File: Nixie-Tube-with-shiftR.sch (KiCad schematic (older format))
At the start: 6 parts

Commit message: finalize schematic, added so16 footprint
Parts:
- removed Q?: 2N2219, TO_SOT_Packages_THT:TO-39-3, symbol 2N2219
- removed R?: 500, symbol R
- removed R?: R, symbol R
- removed U?: TPIC6595, symbol TPIC6595
- added D1: LED_CRGB, nixie-tube-fp:Rgb-Led, symbol LED_CRGB
- added J1: Conn_01x02_Female, Pin_Headers:Pin_Header_Angled_2x01_Pitch2.54mm, symbol Conn_01x02_Female
- added J2: Conn_01x06, Pin_Headers:Pin_Header_Angled_1x06_Pitch2.54mm, symbol Conn_01x06
- added Q1, Q10, Q2, Q3, Q4, Q5, Q6, Q7, Q8, Q9: 2N2219, TO_SOT_Packages_THT:TO-39-3, symbol 2N2219
- added Q11, Q12, Q13: Q_NMOS_DGS, symbol Q_NMOS_DGS
- added R1, R10, R2, R3, R4, R5, R6, R7, R8, R9: 25K, Resistors_SMD:R_0603, symbol R
- added R11, R12, R13: 500, Resistors_SMD:R_0603, symbol R
- added R14, R15, R16, R17, R18, R19, R20, R21, R22, R23: R, Resistors_SMD:R_0603, symbol R
- added U1, U3: 74HC595D, kilibs:SO16, symbol 74HC595D
- J3: renamed from J?; footprint (none) -> Pin_Headers:Pin_Header_Angled_1x02_Pitch2.54mm
- U2: renamed from U?; footprint (none) -> nixie-tube-fp:qs30-1
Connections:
- net labels added: +5V, Blue, Green, Red, n0, n1, n2, n3, n4, n5, n6, n7, n8, n9, s0, s1, s2, s3, s4, s5, s6, s7, s8, s9
- wire segments 8 -> 58
- no-connect marks 0 -> 7
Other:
- note added: "DS0"
- note added: "DS1"
- note added: "MR"
- note added: "OE"
- note added: "SHCP"
- note added: "STCP"

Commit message: associate all footprints, components are outside of board
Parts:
- removed J1: Conn_01x02_Female, Pin_Headers:Pin_Header_Angled_2x01_Pitch2.54mm, symbol Conn_01x02_Female
- removed J2: Conn_01x06, Pin_Headers:Pin_Header_Angled_1x06_Pitch2.54mm, symbol Conn_01x06
- removed J3: Conn_01x02_Female, Pin_Headers:Pin_Header_Angled_1x02_Pitch2.54mm, symbol Conn_01x02_Female
- removed Q1, Q10, Q2, Q3, Q4, Q5, Q6, Q7, Q8, Q9: 2N2219, TO_SOT_Packages_THT:TO-39-3, symbol 2N2219
- added C1, C2: 0.1uF, symbol C
- added D2: Dot_LED, symbol LED
- added J1: Conn_01x05_Male, Pin_Headers:Pin_Header_Angled_1x05_Pitch2.54mm, symbol Conn_01x05_Male
- added J2: Conn_01x01_Female, Socket_Strips:Socket_Strip_Angled_1x01_Pitch2.54mm, symbol Conn_01x01_Female
- added J3: Conn_01x05_Female, Socket_Strips:Socket_Strip_Angled_1x05_Pitch2.54mm, symbol Conn_01x05_Female
- added J4: Conn_01x01_Male, Pin_Headers:Pin_Header_Angled_1x01_Pitch2.54mm, symbol Conn_01x01_Male
- added Q1, Q10, Q2, Q3, Q4, Q5, Q6, Q7, Q8, Q9: MMBTA42LT1, TO_SOT_Packages_SMD:SOT-23, symbol Q_NPN_BEC
- added Q14: MMBTA42LT1, TO_SOT_Packages_SMD:SOT-23, symbol Q_NPN_BCE
- added R24, R25: R, Resistors_SMD:R_0603, symbol R
- added U4: MIC5219-3.3, TO_SOT_Packages_SMD:SOT-23-5, symbol MIC5219-3.3
- Q11, Q12, Q13: value Q_NMOS_DGS -> AO3400; footprint (none) -> TO_SOT_Packages_SMD:SOT-23
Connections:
- net labels added: +3.3V, +9V, 9V, Dot, MOSI, MOSI-OUT, PWREN, SCK
- net labels removed: +5V
- wire segments 58 -> 62
- no-connect marks 7 -> 4
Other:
- note removed: "DS0"
- note removed: "DS1"
- note removed: "MR"
- note removed: "OE"
- note removed: "SHCP"
- note removed: "STCP"
- moved on the sheet: D1, Q11, Q12, Q13, R11, R12, R13

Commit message: change ldo to 5V
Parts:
- removed U4: MIC5219-3.3, TO_SOT_Packages_SMD:SOT-23-5, symbol MIC5219-3.3
- added U?: MIC5219-5.0, TO_SOT_Packages_SMD:SOT-23-5, symbol MIC5219-5.0
- D2: symbol LED -> LED-RESCUE-Nixie-Tube-with-shiftR
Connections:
- net labels added: +5V
- wire segments 62 -> 77
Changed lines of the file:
@@
 EESchema Schematic File Version 2
+LIBS:Nixie-Tube-with-shiftR-rescue
 LIBS:power
 LIBS:device
 LIBS:switches
 LIBS:relays
-LIBS:motors
 LIBS:transistors
 LIBS:conn
@@
 s1
 Wire Wire Line
-	4050 3125 7325 3125
+	4050 3125 4800 3125
+Wire Wire Line
+	4800 3125 5650 3125
+Wire Wire Line
+	5650 3125 6500 3125
+Wire Wire Line
+	6500 3125 7325 3125
 Connection ~ 4800 3125
 Connection ~ 5650 3125
@@
 Connection ~ 5575 3775
 Wire Wire Line
-	4350 3775 6950 3775
+	4350 3775 4975 3775
+Wire Wire Line
+	4975 3775 5575 3775
+Wire Wire Line
+	5575 3775 6300 3775
+Wire Wire Line
+	6300 3775 6950 3775
 Connection ~ 4975 3775
 Connection ~ 6300 3775
@@
 	9700 5550 8575 5550
 Wire Wire Line
-	4625 1700 3950 1700
+	4625 1700 4475 1700
+Wire Wire Line
+	4475 1700 3950 1700
 $Comp
 L R R11
@@
 	2050 3850 3325 3850
 Wire Wire Line
-	3325 3950 2050 3950
+	3325 3950 2800 3950
+Wire Wire Line
+	2800 3950 2050 3950
 Wire Wire Line
 	3325 4050 2050 4050
 Wire Wire Line
-	2050 4150 3325 4150
+	2050 4150 2575 4150
+Wire Wire Line
+	2575 4150 3325 4150
 Wire Wire Line
 	4900 4275 5325 4275
@@
 MOSI-OUT
 $Comp
-L LED D2
+L LED-RESCUE-Nixie-Tube-with-shiftR D2
 U 1 1 59E02618
 P 8350 2975
@@
 	4300 5675 4300 5950
 Wire Wire Line
-	3700 5950 4600 5950
+	3700 5950 4300 5950
+Wire Wire Line
+	4300 5950 4600 5950
 Wire Wire Line
 	3700 5950 3700 5675
@@
 	5925 5650 5925 5925
 Wire Wire Line
-	5225 5925 6225 5925
+	5225 5925 5925 5925
+Wire Wire Line
+	5925 5925 6225 5925
 Wire Wire Line
 	5225 5925 5225 5625
@@
 $EndComp
 Wire Wire Line
-	2150 5250 2350 5250
+	2150 5250 2225 5250
+Wire Wire Line
+	2225 5250 2275 5250
+Wire Wire Line
+	2275 5250 2350 5250
 Wire Wire Line
 	2950 5250 3275 5250
 Wire Wire Line
 	3275 5250 3275 5200
-$Comp
-L MIC5219-3.3 U4
-U 1 1 59E0C8AF
-P 2650 5350
-F 0 "U4" H 2500 5575 50  0000 C CNN
-F 1 "MIC5219-3.3" H 2650 5575 50  0000 L CNN
-F 2 "TO_SOT_Packages_SMD:SOT-23-5" H 2650 5675 50  0001 C CNN
-F 3 "" H 2650 5350 50  0001 C CNN
-	1    2650 5350
-	1    0    0    -1
-$EndComp
-$Comp
-L +3.3V #PWR013
-U 1 1 59E0C9EB
-P 3275 5200
-F 0 "#PWR013" H 3275 5050 50  0001 C CNN
-F 1 "+3.3V" H 3275 5340 50  0000 C CNN
-F 2 "" H 3275 5200 50  0001 C CNN
-F 3 "" H 3275 5200 50  0001 C CNN
-	1    3275 5200
-	1    0    0    -1
-$EndComp
 Wire Wire Line
 	2350 5350 2275 5350
@@
 Connection ~ 2225 5250
 Wire Wire Line
-	2225 5750 3050 5750
-Wire Wire Line
-	2650 5650 2650 5775
+	2225 5750 2650 5750
+Wire Wire Line
+	2650 5750 3050 5750
+Wire Wire Line
+	2650 5650 2650 5750
+Wire Wire Line
+	2650 5750 2650 5775
 Connection ~ 2650 5750
 $Comp
@@
 	6525 1175 6525 1700
 Connection ~ 4475 1700
+$Comp
+L MIC5219-5.0 U?
+U 1 1 59DFA48B
+P 2650 5350
+F 0 "U?" H 2500 5575 50  0000 C CNN
+F 1 "MIC5219-5.0" H 2650 5575 50  0000 L CNN
+F 2 "TO_SOT_Packages_SMD:SOT-23-5" H 2650 5675 50  0001 C CNN
+F 3 "" H 2650 5350 50  0001 C CNN
+	1    2650 5350
+	1    0    0    -1
+$EndComp
+$Comp
+L +5V #PWR?
+U 1 1 59DFA725
+P 3275 5200
+F 0 "#PWR?" H 3275 5050 50  0001 C CNN
+F 1 "+5V" H 3275 5340 50  0000 C CNN
+F 2 "" H 3275 5200 50  0000 C CNN
+F 3 "" H 3275 5200 50  0000 C CNN
+	1    3275 5200
+	1    0    0    -1
+$EndComp
 $EndSCHEMATC

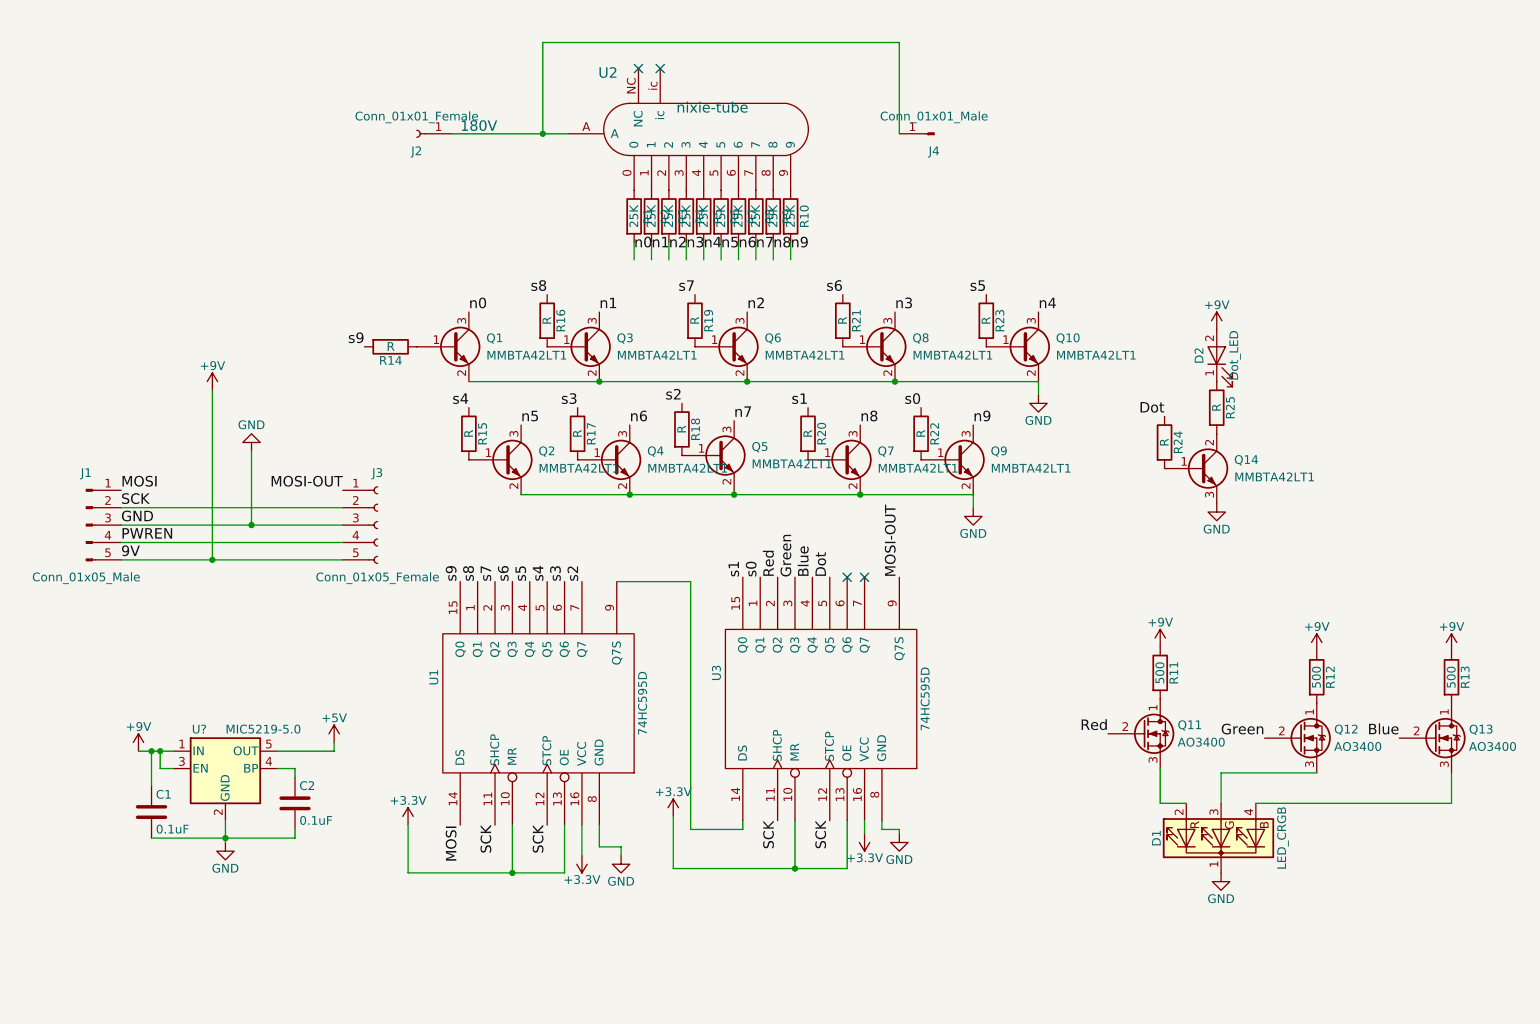
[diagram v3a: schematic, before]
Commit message: rearrange resistor to vertical
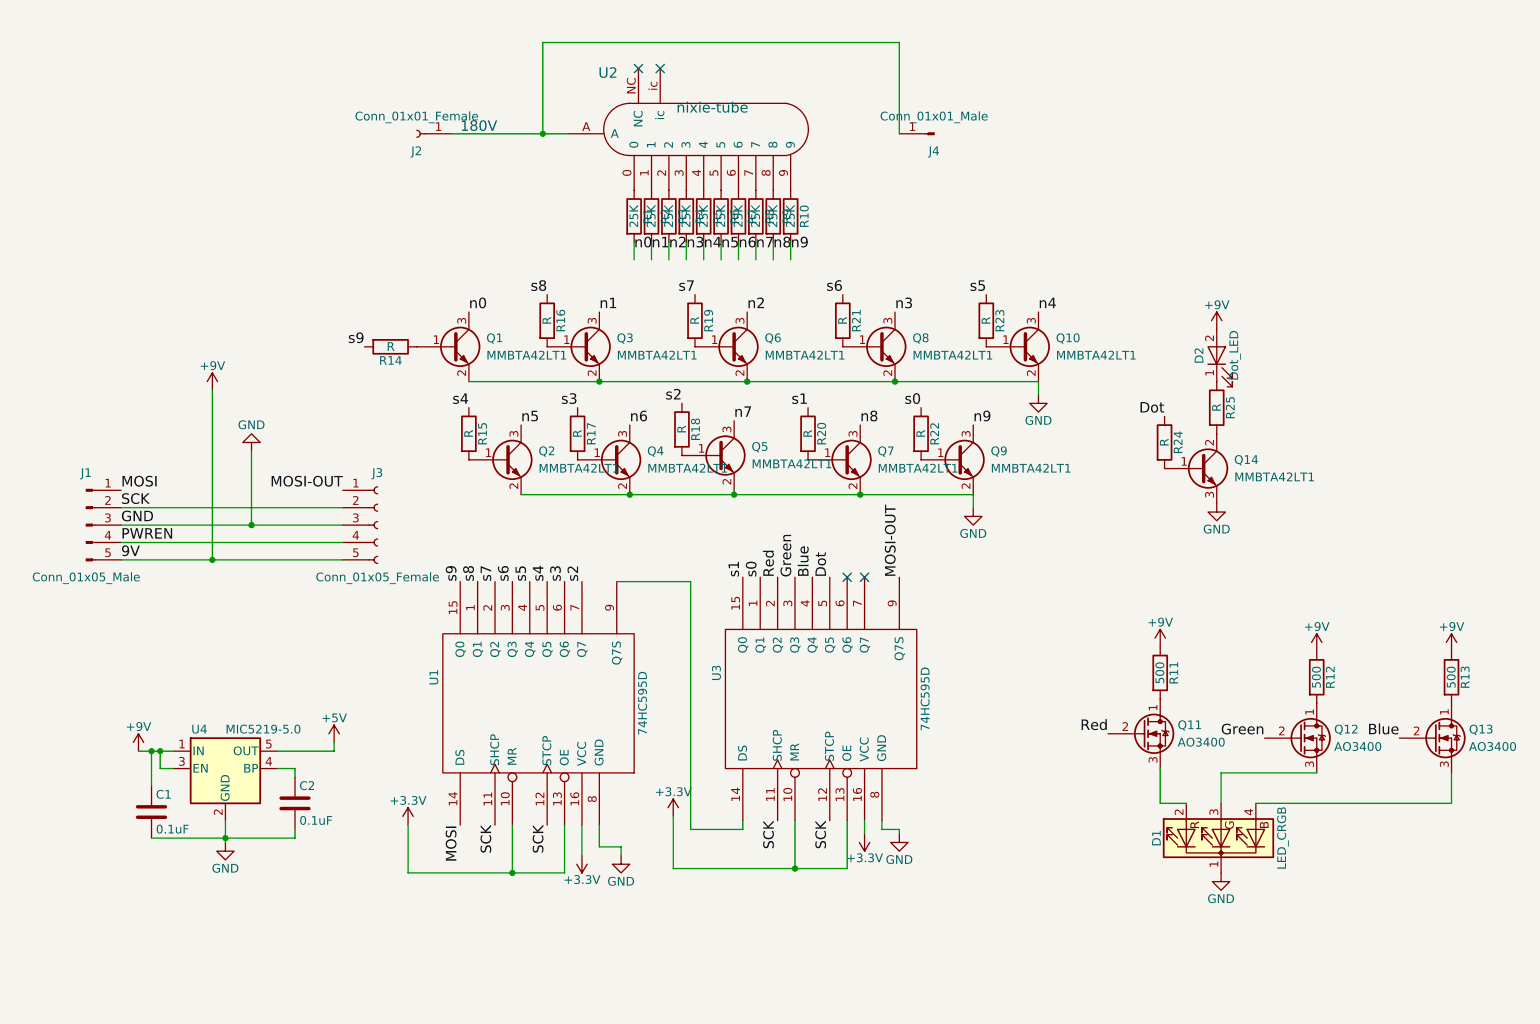
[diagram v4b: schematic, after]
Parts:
- gave numbers to parts that had none: 1
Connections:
- wire segments 77 -> 62
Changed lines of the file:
@@
 LIBS:switches
 LIBS:relays
+LIBS:motors
 LIBS:transistors
 LIBS:conn
@@
 s1
 Wire Wire Line
-	4050 3125 4800 3125
-Wire Wire Line
-	4800 3125 5650 3125
-Wire Wire Line
-	5650 3125 6500 3125
-Wire Wire Line
-	6500 3125 7325 3125
+	4050 3125 7325 3125
 Connection ~ 4800 3125
 Connection ~ 5650 3125
@@
 	7325 3125 7325 3200
 $Comp
-L GND #PWR01
+L GND #PWR13
 U 1 1 59DF0537
 P 7325 3200
-F 0 "#PWR01" H 7325 2950 50  0001 C CNN
+F 0 "#PWR13" H 7325 2950 50  0001 C CNN
 F 1 "GND" H 7325 3050 50  0000 C CNN
 F 2 "" H 7325 3200 50  0001 C CNN
@@
 Connection ~ 5575 3775
 Wire Wire Line
-	4350 3775 4975 3775
-Wire Wire Line
-	4975 3775 5575 3775
-Wire Wire Line
-	5575 3775 6300 3775
-Wire Wire Line
-	6300 3775 6950 3775
+	4350 3775 6950 3775
 Connection ~ 4975 3775
 Connection ~ 6300 3775
@@
 	6950 3775 6950 3850
 $Comp
-L GND #PWR02
+L GND #PWR12
 U 1 1 59DF0997
 P 6950 3850
-F 0 "#PWR02" H 6950 3600 50  0001 C CNN
+F 0 "#PWR12" H 6950 3600 50  0001 C CNN
 F 1 "GND" H 6950 3700 50  0000 C CNN
 F 2 "" H 6950 3850 50  0001 C CNN
@@
 	4925 5800 4925 5850
 $Comp
-L GND #PWR03
+L GND #PWR8
 U 1 1 59DEF495
 P 4925 5850
-F 0 "#PWR03" H 4925 5600 50  0001 C CNN
+F 0 "#PWR8" H 4925 5600 50  0001 C CNN
 F 1 "GND" H 4925 5700 50  0000 C CNN
 F 2 "" H 4925 5850 50  0001 C CNN
@@
 	6325 5650 6325 5725
 $Comp
-L GND #PWR04
+L GND #PWR11
 U 1 1 59DEFAF9
 P 6525 5725
-F 0 "#PWR04" H 6525 5475 50  0001 C CNN
+F 0 "#PWR11" H 6525 5475 50  0001 C CNN
 F 1 "GND" H 6525 5575 50  0000 C CNN
 F 2 "" H 6525 5725 50  0001 C CNN
@@
 $EndComp
 $Comp
-L GND #PWR05
+L GND #PWR17
 U 1 1 59DF166A
 P 8375 5950
-F 0 "#PWR05" H 8375 5700 50  0001 C CNN
+F 0 "#PWR17" H 8375 5700 50  0001 C CNN
 F 1 "GND" H 8375 5800 50  0000 C CNN
 F 2 "" H 8375 5950 50  0001 C CNN
@@
 	9700 5550 8575 5550
 Wire Wire Line
-	4625 1700 4475 1700
-Wire Wire Line
-	4475 1700 3950 1700
+	3950 1700 4625 1700
 $Comp
 L R R11
@@
 	2050 3850 3325 3850
 Wire Wire Line
-	3325 3950 2800 3950
-Wire Wire Line
-	2800 3950 2050 3950
+	2050 3950 3325 3950
 Wire Wire Line
 	3325 4050 2050 4050
 Wire Wire Line
-	2050 4150 2575 4150
-Wire Wire Line
-	2575 4150 3325 4150
+	2050 4150 3325 4150
 Wire Wire Line
 	4900 4275 5325 4275
@@
 Dot
 $Comp
-L GND #PWR06
+L GND #PWR16
 U 1 1 59E03A8E
 P 8350 3825
-F 0 "#PWR06" H 8350 3575 50  0001 C CNN
+F 0 "#PWR16" H 8350 3575 50  0001 C CNN
 F 1 "GND" H 8350 3675 50  0000 C CNN
 F 2 "" H 8350 3825 50  0001 C CNN
@@
 	4300 5675 4300 5950
 Wire Wire Line
-	3700 5950 4300 5950
-Wire Wire Line
-	4300 5950 4600 5950
+	3700 5950 4600 5950
 Wire Wire Line
 	3700 5950 3700 5675
@@
 	5925 5650 5925 5925
 Wire Wire Line
-	5225 5925 5925 5925
-Wire Wire Line
-	5925 5925 6225 5925
+	5225 5925 6225 5925
 Wire Wire Line
 	5225 5925 5225 5625
@@
 Connection ~ 5925 5925
 $Comp
-L +9V #PWR07
+L +9V #PWR2
 U 1 1 59E07785
 P 2575 3175
-F 0 "#PWR07" H 2575 3025 50  0001 C CNN
+F 0 "#PWR2" H 2575 3025 50  0001 C CNN
 F 1 "+9V" H 2575 3315 50  0000 C CNN
 F 2 "" H 2575 3175 50  0001 C CNN
@@
 Connection ~ 2575 4150
 $Comp
-L GND #PWR08
+L GND #PWR4
 U 1 1 59E07C89
 P 2800 3525
-F 0 "#PWR08" H 2800 3275 50  0001 C CNN
+F 0 "#PWR4" H 2800 3275 50  0001 C CNN
 F 1 "GND" H 2800 3375 50  0000 C CNN
 F 2 "" H 2800 3525 50  0001 C CNN
@@
 Connection ~ 2800 3950
 $Comp
-L +9V #PWR09
+L +9V #PWR14
 U 1 1 59E08805
 P 8025 4650
-F 0 "#PWR09" H 8025 4500 50  0001 C CNN
+F 0 "#PWR14" H 8025 4500 50  0001 C CNN
 F 1 "+9V" H 8025 4790 50  0000 C CNN
 F 2 "" H 8025 4650 50  0001 C CNN
@@
 $EndComp
 $Comp
-L +9V #PWR010
+L +9V #PWR18
 U 1 1 59E088D3
 P 8925 4675
-F 0 "#PWR010" H 8925 4525 50  0001 C CNN
+F 0 "#PWR18" H 8925 4525 50  0001 C CNN
 F 1 "+9V" H 8925 4815 50  0000 C CNN
 F 2 "" H 8925 4675 50  0001 C CNN
@@
 $EndComp
 $Comp
-L +9V #PWR011
+L +9V #PWR19
 U 1 1 59E0896B
 P 9700 4675
-F 0 "#PWR011" H 9700 4525 50  0001 C CNN
+F 0 "#PWR19" H 9700 4525 50  0001 C CNN
 F 1 "+9V" H 9700 4815 50  0000 C CNN
 F 2 "" H 9700 4675 50  0001 C CNN
@@
 $EndComp
 $Comp
-L +9V #PWR012
+L +9V #PWR1
 U 1 1 59E0C504
 P 2150 5250
-F 0 "#PWR012" H 2150 5100 50  0001 C CNN
+F 0 "#PWR1" H 2150 5100 50  0001 C CNN
 F 1 "+9V" H 2150 5390 50  0000 C CNN
 F 2 "" H 2150 5250 50  0001 C CNN
@@
 $EndComp
 Wire Wire Line
-	2150 5250 2225 5250
-Wire Wire Line
-	2225 5250 2275 5250
-Wire Wire Line
-	2275 5250 2350 5250
+	2150 5250 2350 5250
 Wire Wire Line
 	2950 5250 3275 5250
@@
 Connection ~ 2275 5250
 $Comp
-L GND #PWR014
+L GND #PWR3
 U 1 1 59E0D231
 P 2650 5775
-F 0 "#PWR014" H 2650 5525 50  0001 C CNN
+F 0 "#PWR3" H 2650 5525 50  0001 C CNN
 F 1 "GND" H 2650 5625 50  0000 C CNN
 F 2 "" H 2650 5775 50  0001 C CNN
@@
 $EndComp
 $Comp
-L +3.3V #PWR015
+L +3.3V #PWR6
 U 1 1 59E0E086
 P 3700 5675
-F 0 "#PWR015" H 3700 5525 50  0001 C CNN
+F 0 "#PWR6" H 3700 5525 50  0001 C CNN
 F 1 "+3.3V" H 3700 5815 50  0000 C CNN
 F 2 "" H 3700 5675 50  0001 C CNN
@@
 $EndComp
 $Comp
-L +3.3V #PWR016
+L +3.3V #PWR9
 U 1 1 59E0E12B
 P 5225 5625
-F 0 "#PWR016" H 5225 5475 50  0001 C CNN
+F 0 "#PWR9" H 5225 5475 50  0001 C CNN
 F 1 "+3.3V" H 5225 5765 50  0000 C CNN
 F 2 "" H 5225 5625 50  0001 C CNN
@@
 $EndComp
 $Comp
-L +3.3V #PWR017
+L +3.3V #PWR7
 U 1 1 59E0E267
 P 4700 5850
-F 0 "#PWR017" H 4700 5700 50  0001 C CNN
+F 0 "#PWR7" H 4700 5700 50  0001 C CNN
 F 1 "+3.3V" H 4700 5990 50  0000 C CNN
 F 2 "" H 4700 5850 50  0001 C CNN
@@
 $EndComp
 $Comp
-L +3.3V #PWR018
+L +3.3V #PWR10
 U 1 1 59E0E3FE
 P 6325 5725
-F 0 "#PWR018" H 6325 5575 50  0001 C CNN
+F 0 "#PWR10" H 6325 5575 50  0001 C CNN
 F 1 "+3.3V" H 6325 5865 50  0000 C CNN
 F 2 "" H 6325 5725 50  0001 C CNN
@@
 Connection ~ 2225 5250
 Wire Wire Line
-	2225 5750 2650 5750
-Wire Wire Line
-	2650 5750 3050 5750
-Wire Wire Line
-	2650 5650 2650 5750
-Wire Wire Line
-	2650 5750 2650 5775
+	2225 5750 3050 5750
+Wire Wire Line
+	2650 5650 2650 5775
 Connection ~ 2650 5750
 $Comp
@@
 	3050 5750 3050 5700
 $Comp
-L +9V #PWR019
+L +9V #PWR15
 U 1 1 59E167E2
 P 8350 2825
-F 0 "#PWR019" H 8350 2675 50  0001 C CNN
+F 0 "#PWR15" H 8350 2675 50  0001 C CNN
 F 1 "+9V" H 8350 2965 50  0000 C CNN
 F 2 "" H 8350 2825 50  0001 C CNN
@@
 Connection ~ 4475 1700
 $Comp
-L MIC5219-5.0 U?
+L MIC5219-5.0 U4
 U 1 1 59DFA48B
 P 2650 5350
-F 0 "U?" H 2500 5575 50  0000 C CNN
+F 0 "U4" H 2500 5575 50  0000 C CNN
 F 1 "MIC5219-5.0" H 2650 5575 50  0000 L CNN
 F 2 "TO_SOT_Packages_SMD:SOT-23-5" H 2650 5675 50  0001 C CNN
@@
 $EndComp
 $Comp
-L +5V #PWR?
+L +5V #PWR5
 U 1 1 59DFA725
 P 3275 5200
-F 0 "#PWR?" H 3275 5050 50  0001 C CNN
+F 0 "#PWR5" H 3275 5050 50  0001 C CNN
 F 1 "+5V" H 3275 5340 50  0000 C CNN
 F 2 "" H 3275 5200 50  0000 C CNN

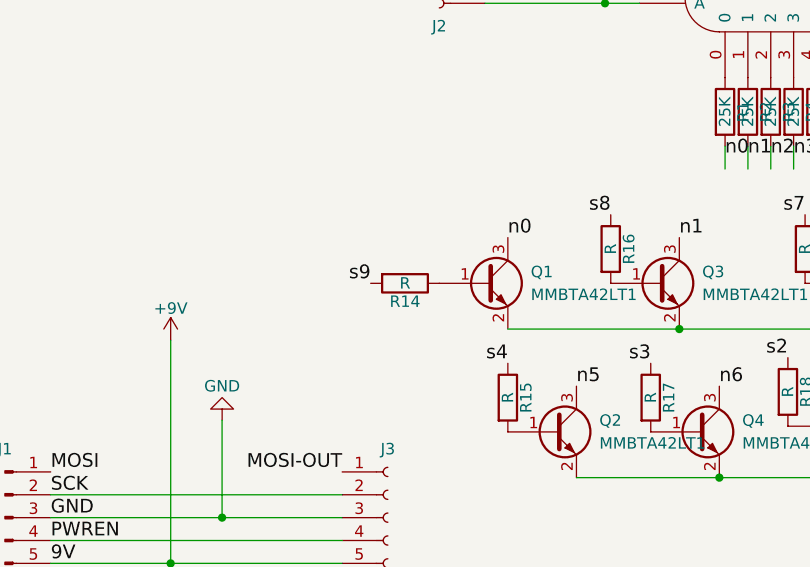
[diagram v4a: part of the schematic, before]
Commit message: routed number 0-9
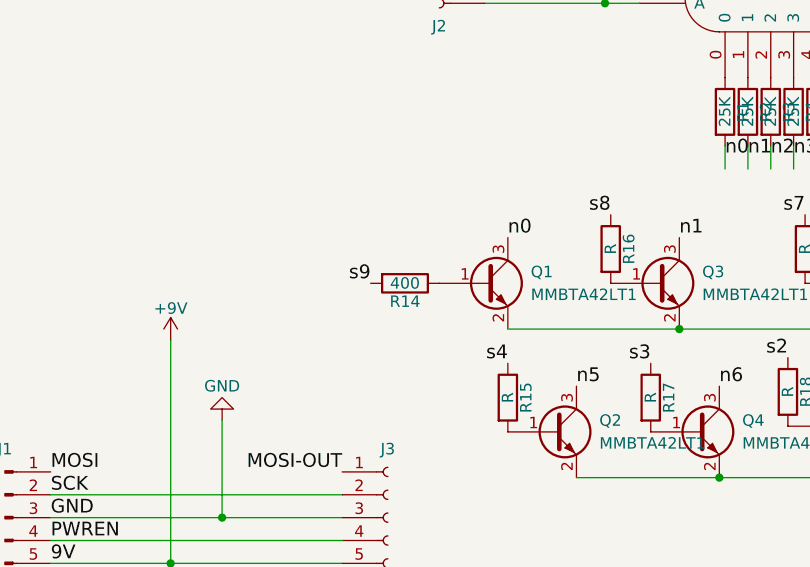
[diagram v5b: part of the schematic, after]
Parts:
- R14: value R -> 400
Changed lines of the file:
@@
 P 3600 2925
 F 0 "R14" V 3680 2925 50  0000 C CNN
-F 1 "R" V 3600 2925 50  0000 C CNN
+F 1 "400" V 3600 2925 50  0000 C CNN
 F 2 "Resistors_SMD:R_0603" V 3530 2925 50  0001 C CNN
 F 3 "" H 3600 2925 50  0001 C CNN
